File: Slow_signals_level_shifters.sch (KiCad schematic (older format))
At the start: 14 parts, among them IC3 TCA9406DCUR, U3 SN74AVCH16T245_DGV_48

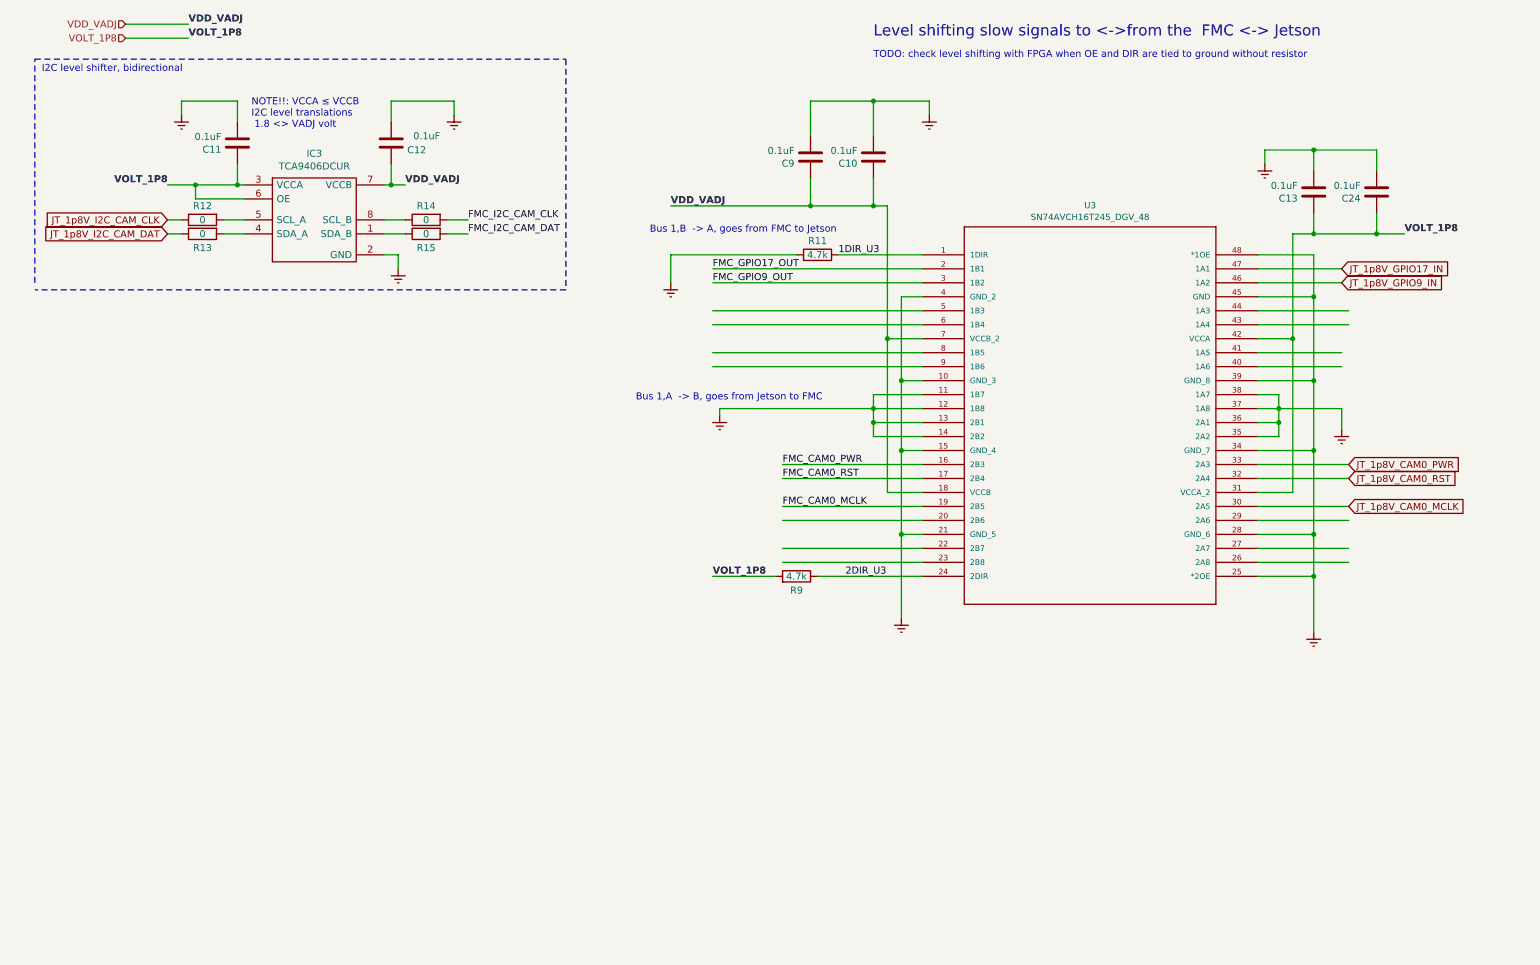
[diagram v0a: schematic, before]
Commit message: added enable line for slow signals
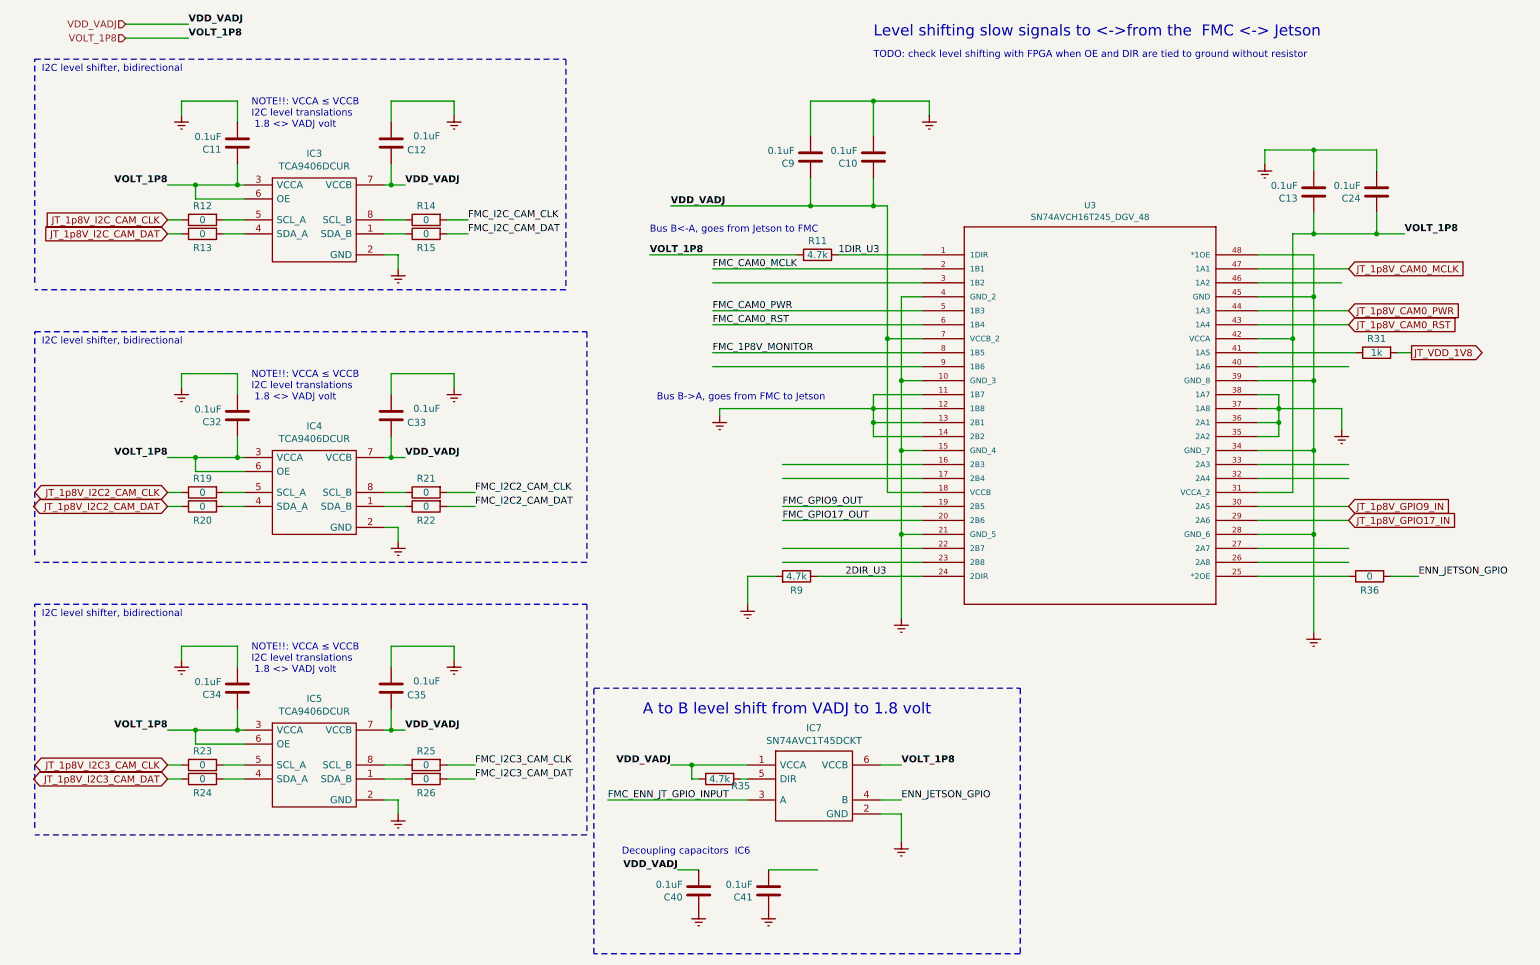
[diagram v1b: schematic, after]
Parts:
- added C32, C33, C34, C35, C40, C41: 0.1uF, Capacitors_SMD:C_0402, symbol FMC_MIPI_v2:C
- added IC4, IC5: TCA9406DCUR, FMC_MIPI_v2_sym:SOP50P310X90-8N, symbol FMC_MIPI_v2:TCA9406DCUR
- added IC7: SN74AVC1T45DCKT, FMC_MIPI_v2_sym:SOT65P210X110-6N, symbol FMC_MIPI_v2:SN74AVC1T45DCKT
- added R19, R20, R21, R22, R23, R24, R25, R26, R36: 0, Resistors_SMD:R_0805, symbol Device:R
- added R31: 1k, Resistors_SMD:R_0805, symbol Device:R
- added R35: 4.7k, Resistors_SMD:R_0805, symbol Device:R
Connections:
- net labels added: ENN_JETSON_GPIO, FMC_1P8V_MONITOR, FMC_ENN_JT_GPIO_INPUT, FMC_I2C2_CAM_CLK, FMC_I2C2_CAM_DAT, FMC_I2C3_CAM_CLK, FMC_I2C3_CAM_DAT, JT_1p8V_I2C2_CAM_CLK, JT_1p8V_I2C2_CAM_DAT, JT_1p8V_I2C3_CAM_CLK, JT_1p8V_I2C3_CAM_DAT, JT_VDD_1V8
- wire segments 122 -> 185
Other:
- note added: "A to B level shift from VADJ to 1.8 volt"
- note added: "Bus B->A, goes from FMC to Jetson"
- note added: "Bus B<-A, goes from Jetson to FMC"
- note added: "Decoupling capacitors IC6"
- note removed: "Bus 1,A -> B, goes from Jetson to FMC"
- note removed: "Bus 1,B -> A, goes from FMC to Jetson"

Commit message: Finished initial placement
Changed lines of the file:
@@
 Wire Wire Line
 	10250 4800 10450 4800
+Text Label 6150 6900 0    50   ~ 10
+VOLT_1P8
 $EndSCHEMATC

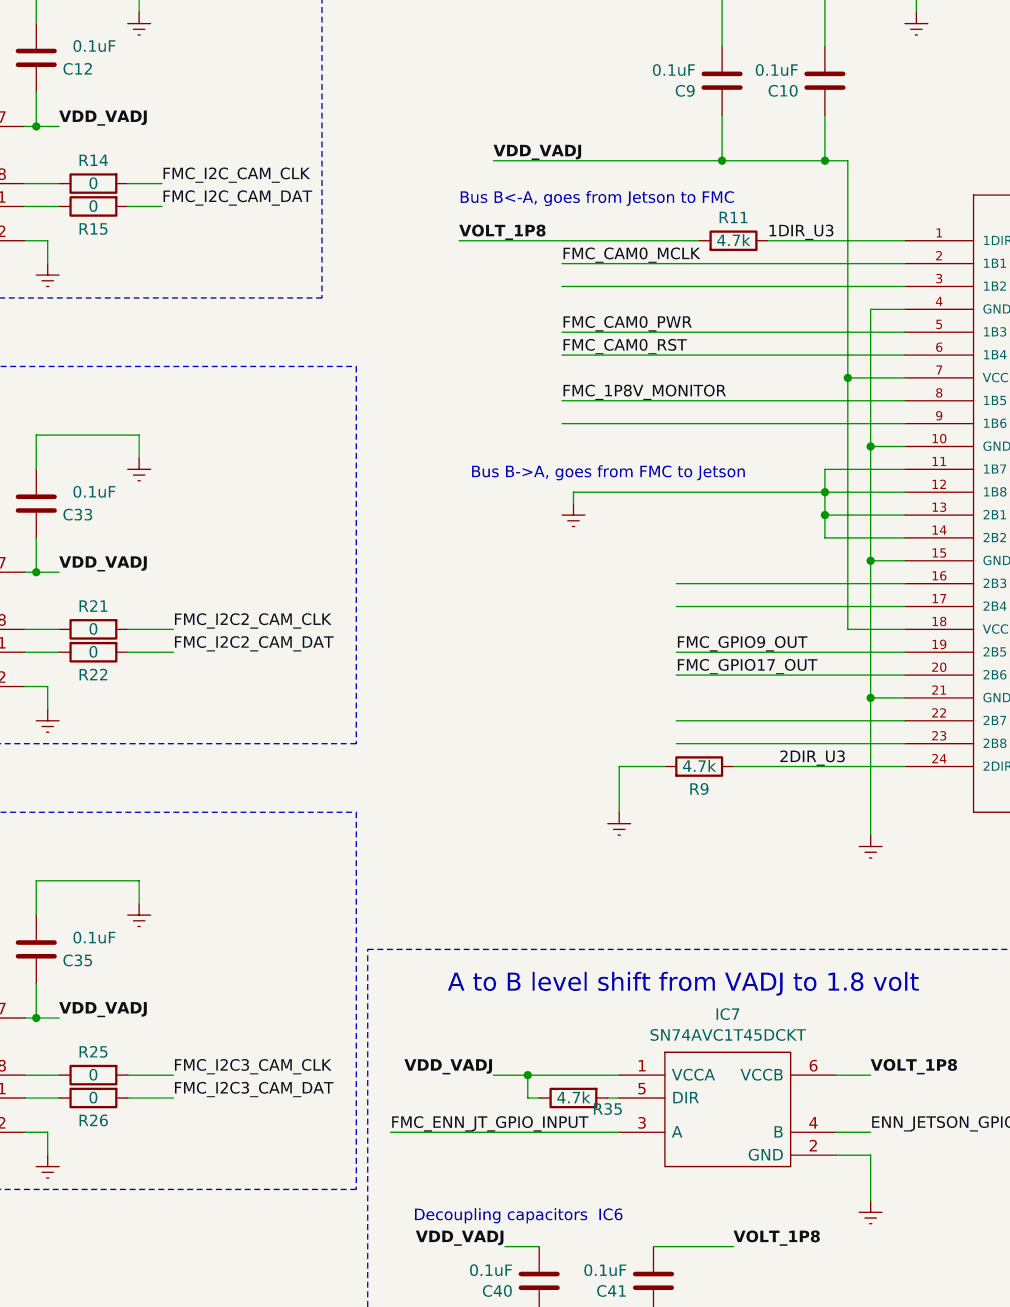
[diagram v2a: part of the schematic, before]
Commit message: Added dummy nets to FMC connector
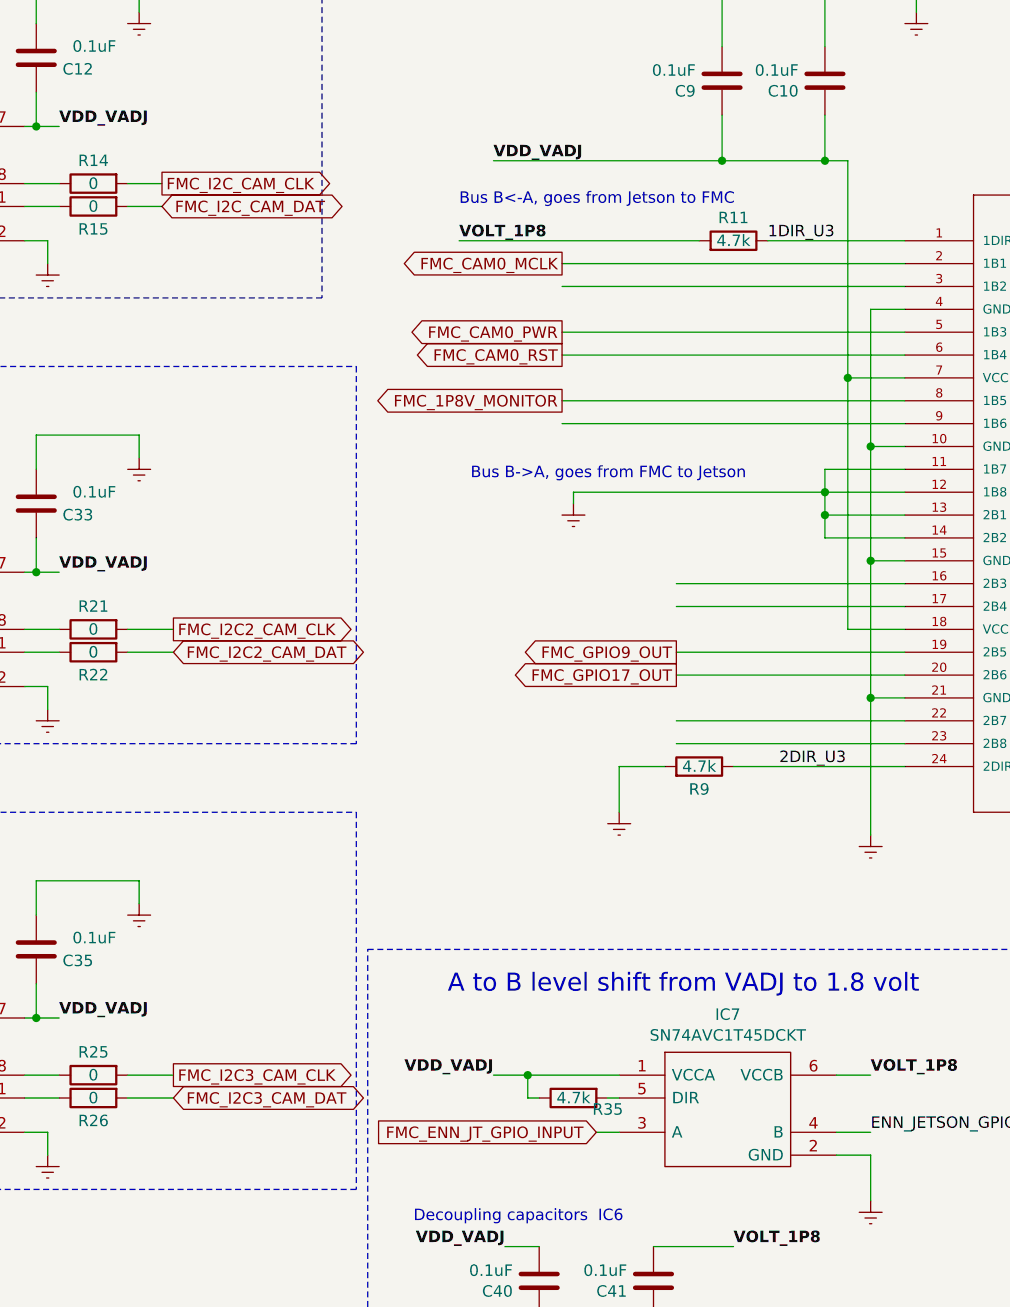
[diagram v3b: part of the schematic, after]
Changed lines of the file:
@@
 Text Label 3200 2000 0    50   ~ 10
 VDD_VADJ
-Text Label 3650 2250 0    50   ~ 0
-FMC_I2C_CAM_CLK
-Text Label 3650 2350 0    50   ~ 0
-FMC_I2C_CAM_DAT
 $Comp
 L FMC_MIPI_v2:C C?
@@
 Text Label 10350 2350 0    50   ~ 10
 VOLT_1P8
-Text Label 5900 4400 0    50   ~ 0
-FMC_GPIO17_OUT
-Text Label 5900 4300 0    50   ~ 0
-FMC_GPIO9_OUT
 Text GLabel 9950 4400 2    50   Input ~ 0
 JT_1p8V_GPIO17_IN
@@
 Wire Wire Line
 	3500 2350 3650 2350
-Text Label 5400 2900 0    50   ~ 0
-FMC_CAM0_PWR
-Text Label 5400 3000 0    50   ~ 0
-FMC_CAM0_RST
-Text Label 5400 2600 0    50   ~ 0
-FMC_CAM0_MCLK
 Wire Wire Line
 	6150 4800 6900 4800
@@
 Text Label 3200 3950 0    50   ~ 10
 VDD_VADJ
-Text Label 3700 4200 0    50   ~ 0
-FMC_I2C2_CAM_CLK
-Text Label 3700 4300 0    50   ~ 0
-FMC_I2C2_CAM_DAT
 $Comp
 L FMC_MIPI_v2:C C?
@@
 Text Label 3200 5900 0    50   ~ 10
 VDD_VADJ
-Text Label 3700 6150 0    50   ~ 0
-FMC_I2C3_CAM_CLK
-Text Label 3700 6250 0    50   ~ 0
-FMC_I2C3_CAM_DAT
 $Comp
 L FMC_MIPI_v2:C C?
@@
 Wire Wire Line
 	10300 3200 10400 3200
-Text Label 5400 3200 0    50   ~ 0
-FMC_1P8V_MONITOR
 Text Label 4950 2500 0    50   ~ 10
 VOLT_1P8
 Wire Wire Line
 	6000 2500 4950 2500
-Text Label 4650 6400 0    50   ~ 0
-FMC_ENN_JT_GPIO_INPUT
 Wire Wire Line
 	9700 4500 9700 5200
@@
 VOLT_1P8
 Wire Wire Line
-	4650 6400 5650 6400
+	5550 6400 5650 6400
 Text Label 10450 4800 0    50   ~ 0
 ENN_JETSON_GPIO
@@
 Text Label 6150 6900 0    50   ~ 10
 VOLT_1P8
+Text GLabel 5400 3200 0    50   Output ~ 0
+FMC_1P8V_MONITOR
+Text GLabel 5400 2900 0    50   Output ~ 0
+FMC_CAM0_PWR
+Text GLabel 5400 2600 0    50   Output ~ 0
+FMC_CAM0_MCLK
+Text GLabel 5400 3000 0    50   Output ~ 0
+FMC_CAM0_RST
+Text GLabel 5900 4300 0    50   Output ~ 0
+FMC_GPIO9_OUT
+Text GLabel 5900 4400 0    50   Output ~ 0
+FMC_GPIO17_OUT
+Text GLabel 3650 2250 2    50   Output ~ 0
+FMC_I2C_CAM_CLK
+Text GLabel 3650 2350 2    50   BiDi ~ 0
+FMC_I2C_CAM_DAT
+Text GLabel 3700 6150 2    50   Output ~ 0
+FMC_I2C3_CAM_CLK
+Text GLabel 3700 6250 2    50   BiDi ~ 0
+FMC_I2C3_CAM_DAT
+Text GLabel 5550 6400 0    50   Input ~ 0
+FMC_ENN_JT_GPIO_INPUT
+Text GLabel 3700 4200 2    50   Output ~ 0
+FMC_I2C2_CAM_CLK
+Text GLabel 3700 4300 2    50   BiDi ~ 0
+FMC_I2C2_CAM_DAT
 $EndSCHEMATC
